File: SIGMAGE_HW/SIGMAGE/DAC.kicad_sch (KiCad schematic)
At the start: 6 parts, among them J20 SJ63073E, J21 SJ63073E, J22 SJ63073E, J23 SJ63073E, U10 PCM5102APWR, U3 PCM5102APWR

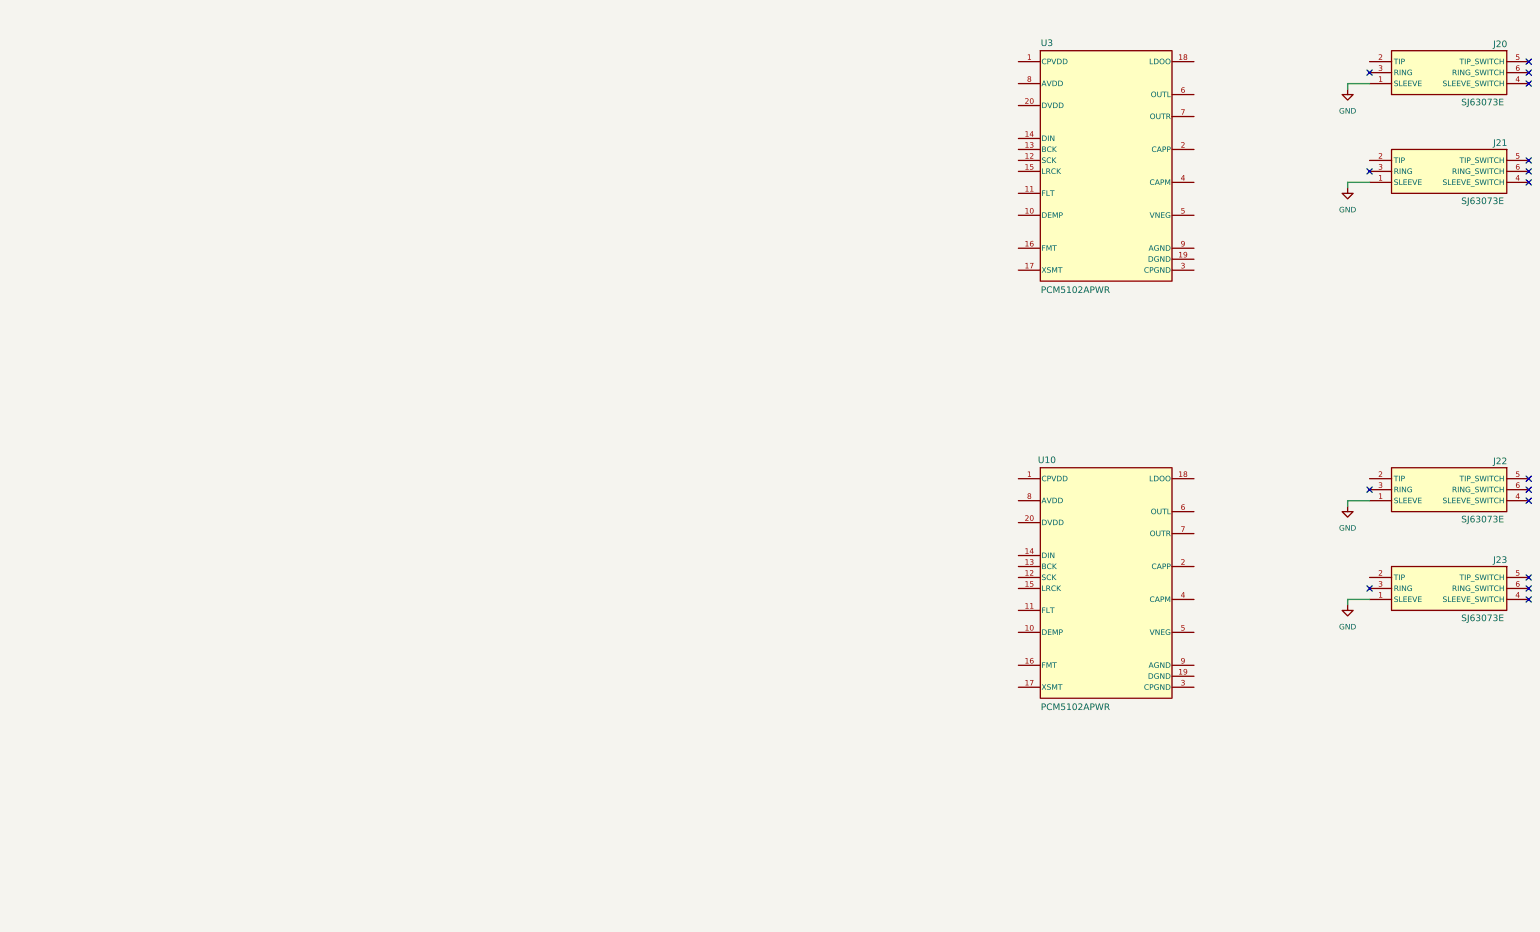
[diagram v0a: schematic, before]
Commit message: More DAC changes
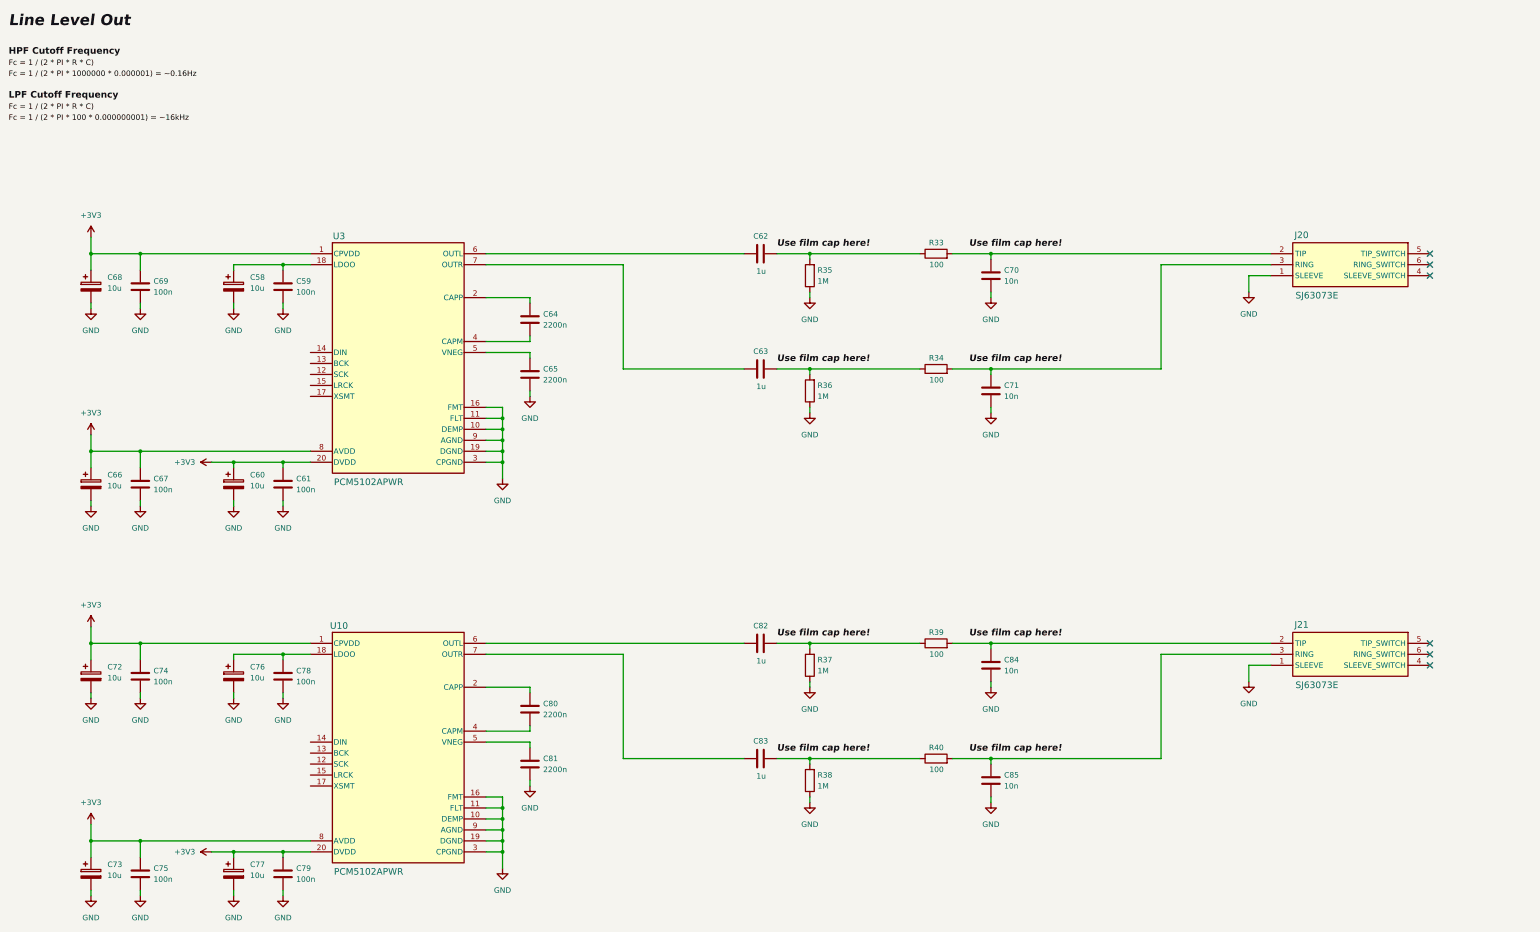
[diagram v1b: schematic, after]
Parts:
- removed J22, J23: SJ63073E, SIGMAGE:SJ63073E, symbol SIGMAGE:SJ63073E
- added C58, C60, C66, C68, C72, C73, C76, C77: 10u, Capacitor_SMD:C_0603_1608Metric, symbol Device:C_Polarized
- added C59, C61, C67, C69, C74, C75, C78, C79: 100n, Capacitor_SMD:C_0603_1608Metric, symbol Device:C
- added C62, C63, C82, C83: 1u, Capacitor_SMD:C_1206_3216Metric, symbol Device:C
- added C64, C65, C80, C81: 2200n, Capacitor_SMD:C_0603_1608Metric, symbol Device:C
- added C70, C71, C84, C85: 10n, Capacitor_SMD:C_0603_1608Metric, symbol Device:C
- added R33, R34, R39, R40: 100, Resistor_SMD:R_0603_1608Metric, symbol Device:R
- added R35, R36, R37, R38: 1M, Resistor_SMD:R_0603_1608Metric, symbol Device:R
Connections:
- net GND: now also U10.10 (DEMP), U10.11 (FLT), U10.16 (FMT), U10.19 (DGND), U10.3 (CPGND), U10.9 (AGND), U3.10 (DEMP), U3.11 (FLT), U3.16 (FMT), U3.19 (DGND), U3.3 (CPGND), U3.9 (AGND), C58.2, C59.2, C60.2, C61.2, C65.2, C66.2, C67.2, C68.2, C69.2, C70.2, C71.2, C72.2, C73.2, C74.2, C75.2, C76.2, C77.2, C78.2, C79.2, C81.2, C84.2, C85.2, R35.1, R36.1, R37.1, R38.1
- net at J20.2 (TIP): now also C70.1, R33.2
- net at J20.3 (RING): now also C71.1, R34.2
- net +3V3: now reaches U10.1 (CPVDD)
- net +3V3: now also U10.20 (DVDD), U10.8 (AVDD), U3.1 (CPVDD), U3.20 (DVDD), U3.8 (AVDD), C60.1, C61.1, C66.1, C67.1, C68.1, C69.1, C72.1, C73.1, C74.1, C75.1, C77.1, C79.1
- net at U10.18 (LDOO): now also C76.1, C78.1
- net at U10.2 (CAPP): now also C80.1
- net at U10.4 (CAPM): now also C80.2
- net at U10.5 (VNEG): now also C81.1
- net at U10.6 (OUTL): now also C82.1
- net at U10.7 (OUTR): now also C83.1
- net at J21.2 (TIP): now also C84.1, R39.2
- net at J21.3 (RING): now also C85.1, R40.2
- net at U3.18 (LDOO): now also C58.1, C59.1
- net at U3.2 (CAPP): now also C64.1
- net at U3.4 (CAPM): now also C64.2
- net at U3.5 (VNEG): now also C65.1
- net at U3.6 (OUTL): now also C62.1
- net at U3.7 (OUTR): now also C63.1
- new net: C63.2, R34.1, R36.2
- new net: C82.2, R37.2, R39.1
- new net: C62.2, R33.1, R35.2
- new net: C83.2, R38.2, R40.1
- no-connect marks 16 -> 6
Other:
- moved on the sheet: J20

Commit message: preps for FPGA
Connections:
- net GND: now also U10.12 (SCK), U3.12 (SCK); no longer U10.10 (DEMP), U10.11 (FLT), U10.16 (FMT), U3.10 (DEMP), U3.11 (FLT), U3.16 (FMT)
- net DAC1_CK: now reaches U3.13 (BCK)
- net DAC1_SD: now reaches U3.14 (DIN)
- net DAC1_WS: now reaches U3.15 (LRCK)
- net DAC1_XSMT: now reaches U3.17 (XSMT)
- net DAC2_CK: now reaches U10.13 (BCK)
- net DAC2_SD: now reaches U10.14 (DIN)
- net DAC2_WS: now reaches U10.15 (LRCK)
- net DAC2_XSMT: now reaches U10.17 (XSMT)
- new net DAC1_DEMP: U3.10 (DEMP)
- new net DAC1_FLT: U3.11 (FLT)
- new net DAC1_FMT: U3.16 (FMT)
- new net DAC2_DEMP: U10.10 (DEMP)
- new net DAC2_FLT: U10.11 (FLT)
- new net DAC2_FMT: U10.16 (FMT)

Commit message: major changes
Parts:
- added C145, C146, C147, C148, C153, C154, C155, C156: 10u, Capacitor_SMD:C_0603_1608Metric, symbol Device:C_Polarized
- added C149, C150, C151, C152, C157, C158, C159, C160: 100n, Capacitor_SMD:C_0603_1608Metric, symbol Device:C
- added C161, C162, C163, C164: 2200n, Capacitor_SMD:C_0603_1608Metric, symbol Device:C
- added C165, C166, C167, C168: 1u, Capacitor_SMD:C_1206_3216Metric, symbol Device:C
- added C169, C170, C171, C172: 10n, Capacitor_SMD:C_0603_1608Metric, symbol Device:C
- added J24, J25: SJ63073E, SIGMAGE:SJ63073E, symbol SIGMAGE:SJ63073E
- added R52, R53, R54, R55: 1M, Resistor_SMD:R_0603_1608Metric, symbol Device:R
- added R63, R64, R65, R66: 100, Resistor_SMD:R_0603_1608Metric, symbol Device:R
- added U20, U21: PCM5102APWR, SIGMAGE:PCM5102APWR, symbol SIGMAGE:PCM5102APWR
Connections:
- net GND: now also C145.2, C146.2, C147.2, C148.2, C149.2, C150.2, C151.2, C152.2, C153.2, C154.2, C155.2, C156.2, C157.2, C158.2, C159.2, C160.2, C162.2, C164.2, C169.2, C170.2, C171.2, C172.2, J24.1 (SLEEVE), J25.1 (SLEEVE), R52.1, R53.1, R54.1, R55.1, U20.12 (SCK), U20.19 (DGND), U20.3 (CPGND), U20.9 (AGND), U21.12 (SCK), U21.19 (DGND), U21.3 (CPGND), U21.9 (AGND)
- net Use film cap here!: now also C82.2, C84.1, J21.2 (TIP), R37.2, R39.1, R39.2
- net +3V3 renamed AVCC_3V3
- net AVCC_3V3: now also C145.1, C146.1, C147.1, C148.1, C149.1, C150.1, C151.1, C152.1, U20.1 (CPVDD), U20.8 (AVDD), U21.1 (CPVDD), U21.8 (AVDD); no longer C60.1, C61.1, C77.1, C79.1, U10.20 (DVDD), U3.20 (DVDD)
- new net: C153.1, C157.1, U20.18 (LDOO)
- new net: C161.1, U20.2 (CAPP)
- new net: C161.2, U20.4 (CAPM)
- new net: C162.1, U20.5 (VNEG)
- new net: C165.1, U20.6 (OUTL)
- new net: C166.1, U20.7 (OUTR)
- new net: C169.1, J24.2 (TIP), R63.2
- new net: C170.1, J24.3 (RING), R64.2
- new net: C166.2, R53.2, R64.1
- new net: C165.2, R52.2, R63.1
- new net: C155.1, C159.1, U21.18 (LDOO)
- new net: C167.2, R54.2, R65.1
- new net: C168.1, U21.7 (OUTR)
- new net: C168.2, R55.2, R66.1
- new net: C163.1, U21.2 (CAPP)
- new net: C163.2, U21.4 (CAPM)
- new net: C172.1, J25.3 (RING), R66.2
- new net: C171.1, J25.2 (TIP), R65.2
- new net: C164.1, U21.5 (VNEG)
- new net: C167.1, U21.6 (OUTL)
- new net DAC3_CK: U20.13 (BCK)
- new net DAC3_DEMP: U20.10 (DEMP)
- new net DAC3_FLT: U20.11 (FLT)
- new net DAC3_FMT: U20.16 (FMT)
- new net DAC3_SD: U20.14 (DIN)
- new net DAC3_WS: U20.15 (LRCK)
- new net DAC3_XSMT: U20.17 (XSMT)
- new net DAC4_CK: U21.13 (BCK)
- new net DAC4_DEMP: U21.10 (DEMP)
- new net DAC4_FLT: U21.11 (FLT)
- new net DAC4_FMT: U21.16 (FMT)
- new net DAC4_SD: U21.14 (DIN)
- new net DAC4_WS: U21.15 (LRCK)
- new net DAC4_XSMT: U21.17 (XSMT)
- new net DVCC_3V3: C154.1, C156.1, C158.1, C160.1, C60.1, C61.1, C77.1, C79.1, U10.20 (DVDD), U20.20 (DVDD), U21.20 (DVDD), U3.20 (DVDD)
- no-connect marks 6 -> 12
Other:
- moved on the sheet: C58, C59, C60, C61, C62, C63, C64, C65, C66, C67, C68, C69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

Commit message: changes
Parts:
- C169, C170, C171, C172, C70, C71, C84, C85: value 10n -> 1n
- R33, R34, R39, R40, R63, R64, R65, R66: value 100 -> 6500
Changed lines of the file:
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@@
 		)
 	)
-	(label "Fc = 1 {slash} (2 * PI * 100 * 0.000000001) = ~16kHz"
+	(label "Fc = 1 {slash} (2 * PI * 6500 * 0.000000001) = ~25kHz"
 		(at 17.78 43.18 0)
 		(effects
@@
 		)
 	)
-	(label "Adjust filters up to 25kHz"
-		(at 303.53 133.35 0)
-		(effects
-			(font
-				(size 3.81 3.81)
-				(thickness 0.508)
-				(bold yes)
-				(italic yes)
-				(color 255 0 0 1)
-			)
-			(justify left bottom)
-		)
-	)
 	(label "Use film cap here!"
 		(at 231.14 44.45 0)
@@
 			)
 		)
-		(property "Value" "100"
-			(at 269.748 87.63 90)
+		(property "Value" "6500"
+			(at 270.51 87.63 90)
 			(show_name no)
 			(do_not_autoplace no)
@@
 			)
 		)
-		(property "Value" "10n"
+		(property "Value" "1n"
 			(at 283.718 91.44 0)
 			(show_name no)
@@
 			)
 		)
-		(property "Value" "100"
-			(at 269.748 48.26 90)
+		(property "Value" "6500"
+			(at 270.51 48.26 90)
 			(show_name no)
 			(do_not_autoplace no)
@@
 			)
 		)
-		(property "Value" "10n"
+		(property "Value" "1n"
 			(at 283.718 118.11 0)
 			(show_name no)
@@
 			)
 		)
-		(property "Value" "100"
-			(at 269.748 180.34 90)
+		(property "Value" "6500"
+			(at 270.51 180.34 90)
 			(show_name no)
 			(do_not_autoplace no)
@@
 			)
 		)
-		(property "Value" "10n"
+		(property "Value" "1n"
 			(at 283.718 157.48 0)
 			(show_name no)
@@
 			)
 		)
-		(property "Value" "10n"
+		(property "Value" "1n"
 			(at 283.718 25.4 0)
 			(show_name no)
@@
 			)
 		)
-		(property "Value" "100"
-			(at 269.748 21.59 90)
+		(property "Value" "6500"
+			(at 270.51 21.59 90)
 			(show_name no)
 			(do_not_autoplace no)
@@
 			)
 		)
-		(property "Value" "10n"
+		(property "Value" "1n"
 			(at 283.718 250.19 0)
 			(show_name no)
@@
 			)
 		)
-		(property "Value" "10n"
+		(property "Value" "1n"
 			(at 283.718 184.15 0)
 			(show_name no)
@@
 			)
 		)
-		(property "Value" "100"
-			(at 269.748 219.71 90)
+		(property "Value" "6500"
+			(at 270.51 219.71 90)
 			(show_name no)
 			(do_not_autoplace no)
@@
 			)
 		)
-		(property "Value" "100"
-			(at 269.748 114.3 90)
+		(property "Value" "6500"
+			(at 270.51 114.3 90)
 			(show_name no)
 			(do_not_autoplace no)
@@
 			)
 		)
-		(property "Value" "100"
-			(at 269.748 153.67 90)
+		(property "Value" "6500"
+			(at 270.51 153.67 90)
 			(show_name no)
 			(do_not_autoplace no)
@@
 			)
 		)
-		(property "Value" "10n"
+		(property "Value" "1n"
 			(at 283.718 52.07 0)
 			(show_name no)
@@
 			)
 		)
-		(property "Value" "10n"
+		(property "Value" "1n"
 			(at 283.718 223.52 0)
 			(show_name no)
@@
 			)
 		)
-		(property "Value" "100"
-			(at 269.748 246.38 90)
+		(property "Value" "6500"
+			(at 270.51 246.38 90)
 			(show_name no)
 			(do_not_autoplace no)

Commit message: finishing up
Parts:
- added C177: 100n, Capacitor_SMD:C_1206_3216Metric, symbol Device:C
- added C178: 10u, Capacitor_SMD:C_1206_3216Metric, symbol Device:C
- added U30: OPA1612AIDRGR, SIGMAGE:OPA1612AIDRGR, symbol SIGMAGE:OPA1612AIDRGR
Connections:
- net GND: now also C177.2, C178.2, U30.4 (V-), U30.9 (EPAD)
- net at C63.1: no longer U3.7 (OUTR)
- net at C62.1: no longer U3.6 (OUTL)
- net Use film cap here!: no longer names the net of C82.2, R37.2, R39.1
- net Use film cap here!: no longer C84.1, J21.2 (TIP), R39.2
- new net: C84.1, J21.2 (TIP), R39.2
- new net: U3.6 (OUTL), U30.3 (+INA)
- new net: U3.7 (OUTR), U30.5 (+INB)
- new net AN_OUT1_L: U30.2 (-INA), U30.7 (OUTB)
- new net AN_OUT1_R: U30.1 (OUTA), U30.6 (-INB)
- new net VCC_5V: C177.1, C178.1, U30.8 (V+)
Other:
- moved on the sheet: C145, C146, C147, C148, C149, C150, C151, C152, C153, C154, C155, C156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

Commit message: almost done
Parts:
- removed C177: 100n, Capacitor_SMD:C_1206_3216Metric, symbol Device:C
- removed C178: 10u, Capacitor_SMD:C_1206_3216Metric, symbol Device:C
- removed U30: OPA1612AIDRGR, SIGMAGE:OPA1612AIDRGR, symbol SIGMAGE:OPA1612AIDRGR
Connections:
- net GND: no longer U10.12 (SCK), U20.12 (SCK), U21.12 (SCK), U3.12 (SCK)
- net at C63.1: now also U3.7 (OUTR)
- net at C62.1: now also U3.6 (OUTL)
- new net DAC1_SCK: U3.12 (SCK)
- new net DAC2_SCK: U10.12 (SCK)
- new net DAC3_SCK: U20.12 (SCK)
- new net DAC4_SCK: U21.12 (SCK)

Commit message: finished schematic
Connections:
- net DAC1_CK renamed 0_DAC1_CK
- net DAC1_DEMP renamed 0_DAC1_DEMP
- net DAC1_FLT renamed 0_DAC1_FLT
- net DAC1_FMT renamed 0_DAC1_FMT
- net DAC1_SCK renamed 0_DAC1_SCK
- net DAC1_SD renamed 0_DAC1_SD
- net DAC1_WS renamed 0_DAC1_WS
- net DAC1_XSMT renamed 0_DAC1_XSMT
- net DAC2_CK renamed 0_DAC2_CK
- net DAC2_DEMP renamed 0_DAC2_DEMP
- net DAC2_FLT renamed 0_DAC2_FLT
- net DAC2_FMT renamed 0_DAC2_FMT
- net DAC2_SCK renamed 0_DAC2_SCK
- net DAC2_SD renamed 0_DAC2_SD
- net DAC2_WS renamed 0_DAC2_WS
- net DAC2_XSMT renamed 0_DAC2_XSMT
- net DAC3_CK renamed 0_DAC3_CK
- net DAC3_DEMP renamed 0_DAC3_DEMP
- net DAC3_FLT renamed 0_DAC3_FLT
- net DAC3_FMT renamed 0_DAC3_FMT
- net DAC3_SCK renamed 0_DAC3_SCK
- net DAC3_SD renamed 0_DAC3_SD
- net DAC3_WS renamed 0_DAC3_WS
- net DAC3_XSMT renamed 0_DAC3_XSMT
- net DAC4_CK renamed 0_DAC4_CK
- net DAC4_DEMP renamed 0_DAC4_DEMP
- net DAC4_FLT renamed 0_DAC4_FLT
- net DAC4_FMT renamed 0_DAC4_FMT
- net DAC4_SCK renamed 0_DAC4_SCK
- net DAC4_SD renamed 0_DAC4_SD
- net DAC4_WS renamed 0_DAC4_WS
- net DAC4_XSMT renamed 0_DAC4_XSMT

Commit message: uga uga
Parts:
- C165, C166, C167, C168, C62, C63, C82, C83: footprint Capacitor_SMD:C_1206_3216Metric -> Resistor_SMD:R_0603_1608Metric
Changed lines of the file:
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@@
 			)
 		)
-		(property "Footprint" "Capacitor_SMD:C_1206_3216Metric"
+		(property "Footprint" "Resistor_SMD:R_0603_1608Metric"
 			(at 398.78 161.5948 0)
 			(hide yes)
@@
 			)
 		)
-		(property "Footprint" "Capacitor_SMD:C_1206_3216Metric"
+		(property "Footprint" "Resistor_SMD:R_0603_1608Metric"
 			(at 398.78 223.8248 0)
 			(hide yes)
@@
 			)
 		)
-		(property "Footprint" "Capacitor_SMD:C_1206_3216Metric"
+		(property "Footprint" "Resistor_SMD:R_0603_1608Metric"
 			(at 398.78 72.6948 0)
 			(hide yes)
@@
 			)
 		)
-		(property "Footprint" "Capacitor_SMD:C_1206_3216Metric"
+		(property "Footprint" "Resistor_SMD:R_0603_1608Metric"
 			(at 398.78 311.4548 0)
 			(hide yes)
@@
 			)
 		)
-		(property "Footprint" "Capacitor_SMD:C_1206_3216Metric"
+		(property "Footprint" "Resistor_SMD:R_0603_1608Metric"
 			(at 398.78 46.0248 0)
 			(hide yes)
@@
 			)
 		)
-		(property "Footprint" "Capacitor_SMD:C_1206_3216Metric"
+		(property "Footprint" "Resistor_SMD:R_0603_1608Metric"
 			(at 398.78 338.1248 0)
 			(hide yes)
@@
 			)
 		)
-		(property "Footprint" "Capacitor_SMD:C_1206_3216Metric"
+		(property "Footprint" "Resistor_SMD:R_0603_1608Metric"
 			(at 398.78 250.4948 0)
 			(hide yes)
@@
 			)
 		)
-		(property "Footprint" "Capacitor_SMD:C_1206_3216Metric"
+		(property "Footprint" "Resistor_SMD:R_0603_1608Metric"
 			(at 398.78 134.9248 0)
 			(hide yes)
